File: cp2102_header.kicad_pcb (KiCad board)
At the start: 2 copper layers, 13.3 x 22.9 mm, 24 parts, among them J1 FTDI, J2 USB_B_Micro, J8 mount, Q3 BSS138PS, U2 CP2102N

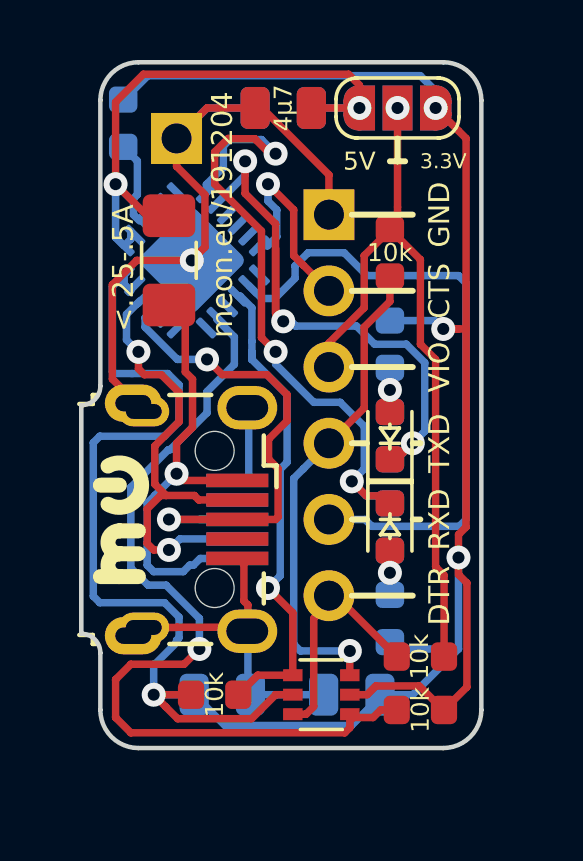
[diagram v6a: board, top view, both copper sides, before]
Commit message: more resistor away from pin
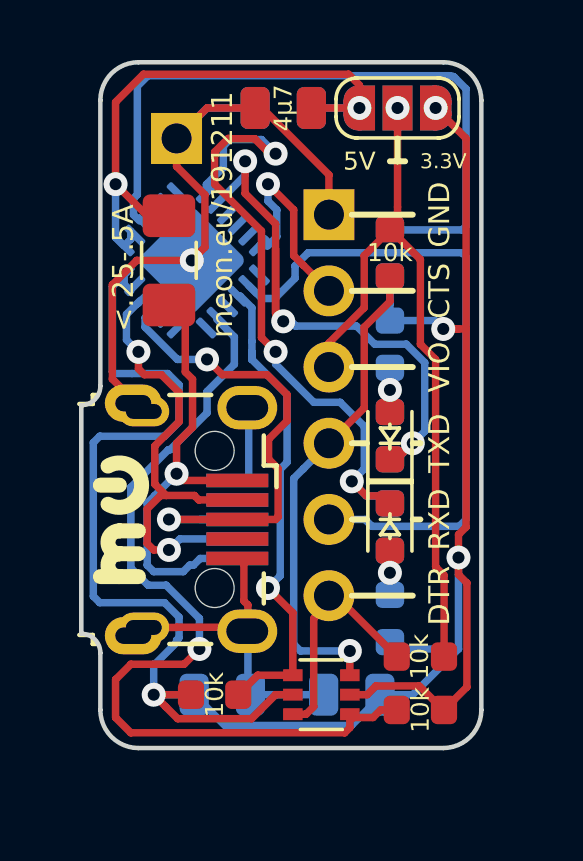
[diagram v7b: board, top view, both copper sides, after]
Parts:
- moved R2 9.88 mm to (88.4, 77.5), turned to 270 degrees
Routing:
- net Net-(R2-Pad1): track 3.17 -> 23.1 mm
- net +3V3: track 85.0 -> 74.8 mm
- net RXD: track 21.4 -> 21.9 mm
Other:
- board text added: "meon.eu/191211"
- board text removed: "meon.eu/191204"
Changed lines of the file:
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@@
     (thickness 1.6)
     (drawings 53)
-    (tracks 357)
+    (tracks 360)
     (zones 0)
     (modules 24)
@@
   )
   (module "Resistor_SMD (GitHub):R_0603_1608Metric_no_lines" (layer B.Cu)
-    (at 79.502 73.152 90)
+    (at 88.392 77.47 270)
     (descr "Resistor SMD 0603 (1608 Metric), square (rectangular) end terminal, IPC_7351 nominal, (Body size source: http://www.tortai-tech.com/upload/download/2011102023233369053.pdf), generated with kicad-footprint-generator")
     (tags resistor)
     (attr smd)
-    (fp_text reference R2 (at 0 1.43 90) (layer B.SilkS) hide
+    (fp_text reference R2 (at 0 1.43 270) (layer B.SilkS) hide
       (effects (font (size 1 1) (thickness 0.15)) (justify mirror))
     )
-    (fp_text value 1k (at 0 0 -180) (layer B.SilkS)
+    (fp_text value 1k (at 0 0) (layer B.SilkS)
       (effects (font (size 0.6 0.6) (thickness 0.125)) (justify mirror))
     )
@@
     (fp_line (start 1.48 0.73) (end 1.48 -0.73) (layer B.CrtYd) (width 0.05))
     (fp_line (start 1.48 -0.73) (end -1.48 -0.73) (layer B.CrtYd) (width 0.05))
-    (fp_text user %R (at 0 0 90) (layer B.Fab)
+    (fp_text user %R (at 0 0 270) (layer B.Fab)
       (effects (font (size 0.4 0.4) (thickness 0.06)) (justify mirror))
     )
-    (pad 1 smd roundrect (at -0.7875 0 90) (size 0.875 0.95) (layers B.Cu B.Paste B.Mask) (roundrect_rratio 0.25)
+    (pad 1 smd roundrect (at -0.7875 0 270) (size 0.875 0.95) (layers B.Cu B.Paste B.Mask) (roundrect_rratio 0.25)
       (net 13 "Net-(R2-Pad1)"))
-    (pad 2 smd roundrect (at 0.7875 0 90) (size 0.875 0.95) (layers B.Cu B.Paste B.Mask) (roundrect_rratio 0.25)
+    (pad 2 smd roundrect (at 0.7875 0 270) (size 0.875 0.95) (layers B.Cu B.Paste B.Mask) (roundrect_rratio 0.25)
       (net 1 +3V3))
     (model ${KISYS3DMOD}/Resistor_SMD.3dshapes/R_0603_1608Metric.wrl
@@
   (gr_line (start 87.122 78.74) (end 89.154 78.74) (layer F.SilkS) (width 0.2))
   (gr_line (start 87.122 76.2) (end 89.154 76.2) (layer F.SilkS) (width 0.2))
-  (gr_text meon.eu/191204 (at 82.804 76.2 90) (layer F.SilkS)
+  (gr_text meon.eu/191211 (at 82.804 76.2 90) (layer F.SilkS)
     (effects (font (size 0.7 0.7) (thickness 0.15)))
   )
@@
     (effects (font (size 0.7 0.7) (thickness 0.15)))
   )
-  (gr_text meon.eu/191204 (at 84.582 93.218) (layer B.SilkS)
+  (gr_text meon.eu/191211 (at 84.582 93.218) (layer B.SilkS)
     (effects (font (size 0.7 0.7) (thickness 0.15)) (justify mirror))
   )
@@
   (segment (start 90.678 90.678) (end 88.9 90.678) (width 0.25) (layer B.Cu) (net 1))
   (segment (start 88.9 90.678) (end 88.392 90.17) (width 0.25) (layer B.Cu) (net 1) (status 20))
-  (segment (start 80.32401 71.56799) (end 79.502 72.39) (width 0.25) (layer B.Cu) (net 1) (status 20))
   (via (at 90.17 80.01) (size 0.8) (drill 0.4) (layers F.Cu B.Cu) (net 1))
   (segment (start 89.408 91.948) (end 90.678 90.678) (width 0.25) (layer B.Cu) (net 1))
-  (segment (start 89.405675 71.56799) (end 80.32401 71.56799) (width 0.25) (layer B.Cu) (net 1))
-  (segment (start 89.916 72.078315) (end 89.405675 71.56799) (width 0.25) (layer B.Cu) (net 1) (status 10))
-  (segment (start 89.916 72.644) (end 89.916 72.078315) (width 0.25) (layer B.Cu) (net 1) (status 30))
   (segment (start 90.678 73.406) (end 89.916 72.644) (width 0.25) (layer F.Cu) (net 1) (status 20))
   (segment (start 90.678 87.63) (end 90.678 90.678) (width 0.25) (layer B.Cu) (net 1))
@@
   (segment (start 79.534097 78.210136) (end 79.534097 78.518097) (width 0.25) (layer B.Cu) (net 1))
   (segment (start 79.534097 78.518097) (end 79.756 78.74) (width 0.25) (layer B.Cu) (net 1))
+  (segment (start 88.392 79.7305) (end 88.392 79.193) (width 0.25) (layer B.Cu) (net 1))
+  (segment (start 88.392 79.193) (end 88.392 78.359) (width 0.25) (layer B.Cu) (net 1))
   (segment (start 83.488 90.235) (end 83.638 90.085) (width 0.25) (layer F.Cu) (net 2) (status 30))
   (segment (start 83.688 90.035) (end 83.638 90.085) (width 0.25) (layer F.Cu) (net 2) (status 30))
@@
   (segment (start 82.22601 77.28599) (end 82.22601 75.53582) (width 0.25) (layer F.Cu) (net 2))
   (segment (start 81.28 74.58981) (end 81.28 73.66) (width 0.25) (layer F.Cu) (net 2))
-  (via (at 79.248 75.184) (size 0.8) (drill 0.4) (layers F.Cu B.Cu) (net 3))
-  (via (at 87.376 72.644) (size 0.8) (drill 0.4) (layers F.Cu B.Cu) (net 3) (status 30))
-  (segment (start 85.852 72.644) (end 85.598 72.39) (width 0.25) (layer B.Cu) (net 3))
   (segment (start 86.36 74.872998) (end 84.131002 72.644) (width 0.25) (layer F.Cu) (net 2))
   (segment (start 86.36 76.2) (end 86.36 74.872998) (width 0.25) (layer F.Cu) (net 2))
@@
   (segment (start 83.8985 72.644) (end 82.296 72.644) (width 0.25) (layer B.Cu) (net 2))
   (segment (start 82.296 72.644) (end 81.28 73.66) (width 0.25) (layer B.Cu) (net 2))
+  (via (at 79.248 75.184) (size 0.8) (drill 0.4) (layers F.Cu B.Cu) (net 3))
+  (via (at 87.376 72.644) (size 0.8) (drill 0.4) (layers F.Cu B.Cu) (net 3) (status 30))
+  (segment (start 85.852 72.644) (end 85.598 72.39) (width 0.25) (layer B.Cu) (net 3))
   (segment (start 87.2005 72.4685) (end 87.376 72.644) (width 0.25) (layer F.Cu) (net 3))
   (segment (start 79.534097 77.237864) (end 79.756 77.015961) (width 0.25) (layer B.Cu) (net 3))
@@
   (segment (start 87.562081 86.36) (end 86.36 86.36) (width 0.25) (layer B.Cu) (net 10) (status 20))
   (segment (start 90.932 86.36) (end 90.70299 86.58901) (width 0.25) (layer B.Cu) (net 10))
-  (segment (start 90.678 78.232) (end 90.932 78.486) (width 0.25) (layer B.Cu) (net 10))
   (segment (start 90.70299 86.58901) (end 87.791091 86.58901) (width 0.25) (layer B.Cu) (net 10))
   (segment (start 90.932 78.486) (end 90.932 86.36) (width 0.25) (layer B.Cu) (net 10))
-  (segment (start 87.63 78.232) (end 90.678 78.232) (width 0.25) (layer B.Cu) (net 10))
-  (segment (start 86.868 77.47) (end 87.63 78.232) (width 0.25) (layer B.Cu) (net 10))
-  (segment (start 85.229095 78.319942) (end 85.229095 77.906442) (width 0.25) (layer B.Cu) (net 10))
-  (segment (start 85.665537 77.47) (end 86.868 77.47) (width 0.25) (layer B.Cu) (net 10))
   (segment (start 87.791091 86.58901) (end 87.562081 86.36) (width 0.25) (layer B.Cu) (net 10))
-  (segment (start 85.229095 77.906442) (end 85.665537 77.47) (width 0.25) (layer B.Cu) (net 10))
-  (segment (start 85.229095 78.319942) (end 84.555037 78.994) (width 0.25) (layer B.Cu) (net 10))
+  (segment (start 90.932 77.597) (end 90.932 78.486) (width 0.25) (layer B.Cu) (net 10))
   (segment (start 84.11866 78.994) (end 84.555037 78.994) (width 0.25) (layer B.Cu) (net 10))
   (segment (start 83.688349 78.563689) (end 84.11866 78.994) (width 0.25) (layer B.Cu) (net 10))
+  (segment (start 84.555037 78.994) (end 85.229095 78.319942) (width 0.25) (layer B.Cu) (net 10))
+  (segment (start 90.805 77.47) (end 90.932 77.597) (width 0.25) (layer B.Cu) (net 10))
+  (segment (start 85.229095 78.319942) (end 85.229095 77.906442) (width 0.25) (layer B.Cu) (net 10))
+  (segment (start 85.229095 77.906442) (end 85.665537 77.47) (width 0.25) (layer B.Cu) (net 10))
+  (segment (start 85.665537 77.47) (end 90.805 77.47) (width 0.25) (layer B.Cu) (net 10))
   (segment (start 83.791687 81.028749) (end 83.791687 80.772) (width 0.25) (layer B.Cu) (net 11))
   (segment (start 84.96301 82.200072) (end 84.96301 84.45499) (width 0.25) (layer B.Cu) (net 11))
@@
   (segment (start 87.056 90.744) (end 85.41 90.744) (width 0.25) (layer B.Cu) (net 12))
   (segment (start 87.056 91.552) (end 87.056 90.744) (width 0.25) (layer F.Cu) (net 12) (status 10))
-  (segment (start 79.756 74.168) (end 79.502 73.914) (width 0.25) (layer B.Cu) (net 13) (status 30))
   (segment (start 79.844871 75.660131) (end 79.844871 76.205119) (width 0.25) (layer B.Cu) (net 13))
   (segment (start 79.973001 75.532001) (end 79.844871 75.660131) (width 0.25) (layer B.Cu) (net 13))
-  (segment (start 79.502 73.9395) (end 79.973001 74.410501) (width 0.25) (layer B.Cu) (net 13))
-  (segment (start 79.973001 74.410501) (end 79.973001 75.532001) (width 0.25) (layer B.Cu) (net 13))
   (segment (start 79.844871 76.205119) (end 80.051876 76.412124) (width 0.25) (layer B.Cu) (net 13))
+  (segment (start 79.973001 75.532001) (end 79.973001 71.918999) (width 0.25) (layer B.Cu) (net 13))
+  (segment (start 90.499932 71.593474) (end 90.549784 71.626784) (width 0.25) (layer B.Cu) (net 13))
+  (segment (start 90.376845 71.56899) (end 90.499932 71.593474) (width 0.25) (layer B.Cu) (net 13))
+  (segment (start 79.973001 71.918999) (end 80.32301 71.56899) (width 0.25) (layer B.Cu) (net 13))
+  (segment (start 80.32301 71.56899) (end 90.376845 71.56899) (width 0.25) (layer B.Cu) (net 13))
+  (segment (start 90.549784 71.626784) (end 90.932 72.009) (width 0.25) (layer B.Cu) (net 13))
+  (segment (start 90.932 72.009) (end 90.932 76.581) (width 0.25) (layer B.Cu) (net 13))
+  (segment (start 90.932 76.581) (end 90.805 76.708) (width 0.25) (layer B.Cu) (net 13))
+  (segment (start 90.805 76.708) (end 88.392 76.708) (width 0.25) (layer B.Cu) (net 13))
   (via (at 80.01 80.772) (size 0.8) (drill 0.4) (layers F.Cu B.Cu) (net 14))
   (via (at 81.026 87.376) (size 0.8) (drill 0.4) (layers F.Cu B.Cu) (net 14))

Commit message: remove 2x pull-up R on tx-only side, tidy-up
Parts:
- removed R31, R34: 10k, Resistor_SMD (GitHub):R_0603_1608Metric_no_lines
- C21: moved to F.Cu
- moved R33 13.5 mm to (88.4, 77.5), turned to 270 degrees
- moved R36 2.51 mm to (88.4, 80.0)
- moved C21 2.29 mm to (84.8, 92.2), turned to 0 degrees
- moved Q3 2.05 mm to (88.1, 91.9), turned to 270 degrees
- moved C22 2.03 mm to (84.8, 92.2)
- moved R21 0.51 mm to (88.4, 80.0)
- moved R22 0.51 mm to (88.4, 90.2)
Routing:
- net VIO: track 24.6 -> 10.2 mm
- net DTR: track 8.04 -> 19.1 mm
- net TXD: track 16.4 -> 18.2 mm
- net U_DTR: track 28.7 -> 27.0 mm
- net GND: track 41.4 -> 42.8 mm
- net Net-(D22-Pad2): track 2.24 -> 3.50 mm
- net U_TXD: track 16.3 -> 17.5 mm
- net +3V3: track 74.8 -> 73.9 mm
- net Net-(D21-Pad2): track 2.23 -> 2.74 mm
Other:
- board text added: "meon.eu/200106"
- board text removed: "meon.eu/191211"
